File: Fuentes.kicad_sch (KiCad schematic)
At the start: 10 parts

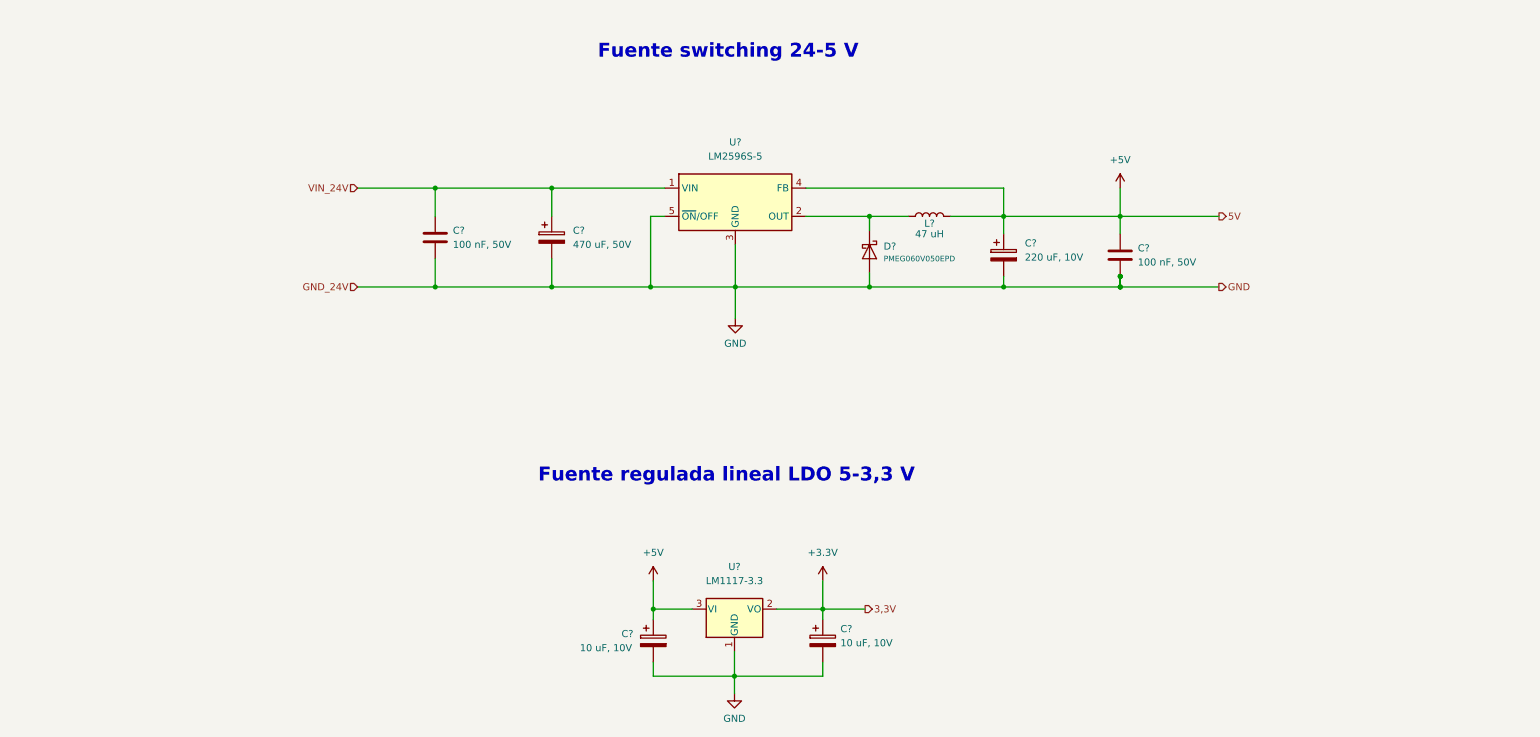
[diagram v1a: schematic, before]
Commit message: Actualización de SCH según placa industrial, y búsqueda de footprints.
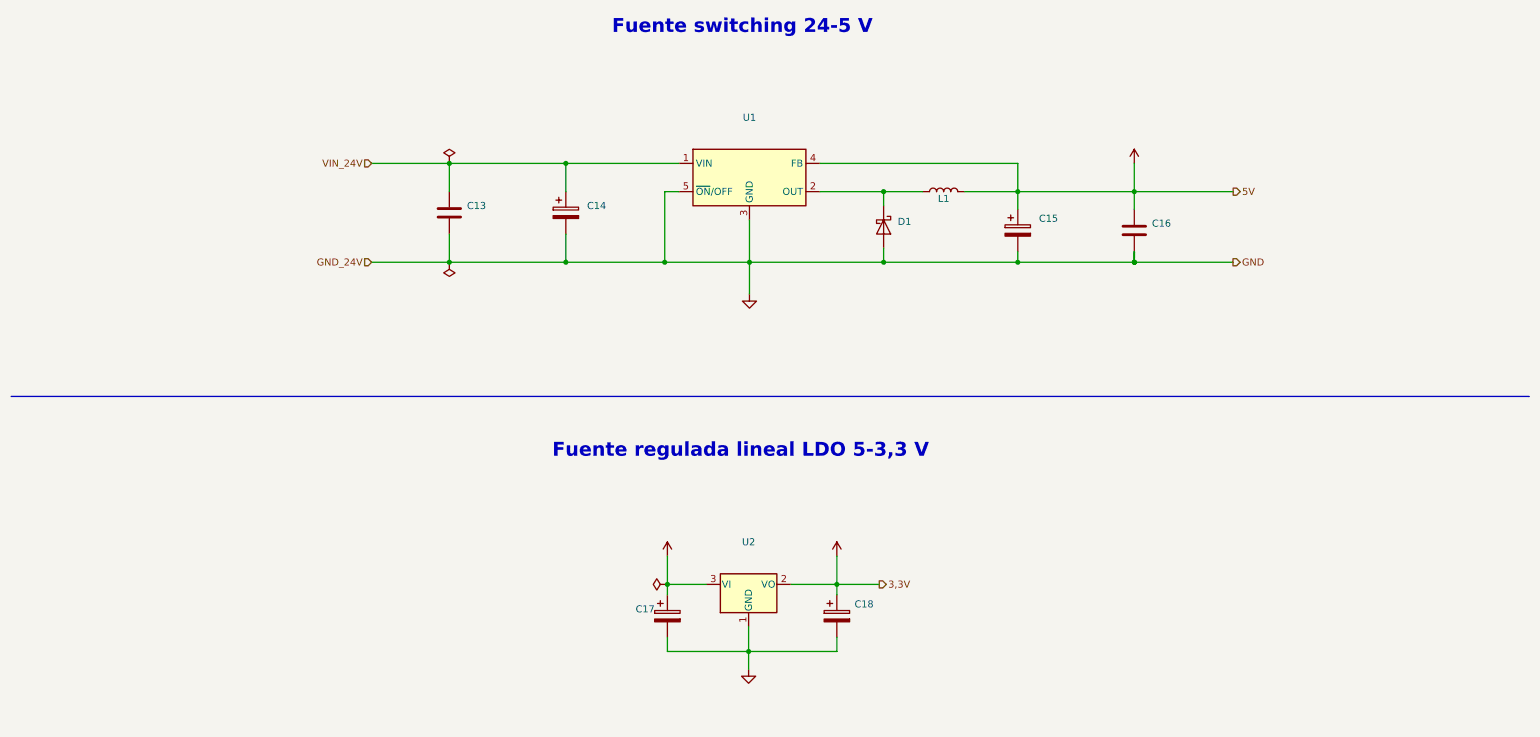
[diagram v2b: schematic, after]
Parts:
- removed C? (x2): 10 uF, 10V, symbol Device:C_Polarized
- removed C? (x2): 100 nF, 50V, symbol Device:C
- removed C?: 220 uF, 10V, symbol Device:C_Polarized
- removed C?: 470 uF, 50V, symbol Device:C_Polarized
- removed D?: PMEG060V050EPD, Package_TO_SOT_SMD:Nexperia_CFP15_SOT-1289, symbol Diode:PMEG060V050EPD
- removed L?: 47 uH, Inductor_SMD:L_0805_2012Metric, symbol Device:L
- removed U?: LM1117-3.3, symbol Regulator_Linear:LM1117-3.3
- removed U?: LM2596S-5, Package_TO_SOT_SMD:TO-263-5_TabPin3, symbol Regulator_Switching:LM2596S-5
- added C13, C16: (no value), Capacitor_SMD:C_0805_2012Metric, symbol Device:C
- added C14, C15: (no value), symbol Device:C_Polarized
- added C17, C18: (no value), Capacitor_SMD:C_0805_2012Metric, symbol Device:C_Polarized
- added D1: (no value), symbol Diode:PMEG060V050EPD
- added L1: (no value), symbol Device:L
- added U1: (no value), symbol Regulator_Switching:LM2596S-5
- added U2: (no value), symbol Regulator_Linear:LM1117-3.3
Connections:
- net +3.3V: now also C18.1, U2.2 (VO)
- net +5V: now also C15.1, C16.1, C17.1, L1.2, U1.4 (FB), U2.3 (VI)
- net GND: now also C13.2, C14.2, C15.2, C16.2, C17.2, C18.2, D1.1 (A), D1.2 (A), U1.3 (GND), U1.5 (~{ON}/OFF), U2.1 (GND)
- net VIN_24V: now also C13.1, C14.1, U1.1 (VIN)
- new net: D1.3 (K), L1.1, U1.2 (OUT)

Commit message: Fin de SCH, config de inicio para PCB
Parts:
- C13, C16: value (none) -> 100 nF, 50V
- C14: value (none) -> 470 uF, 50V; footprint (none) -> UUG1H471MNQ6MS:CAPAE1710X1750N
- C15: value (none) -> 220 uF, 10V; footprint (none) -> TPSE227K010R0100:TPSE227K016R0100V
- C17, C18: value (none) -> 10 uF, 10V
- D1: value (none) -> PMEG060V050EPD; footprint (none) -> Package_TO_SOT_SMD:Nexperia_CFP15_SOT-1289
- L1: value (none) -> 47 uH; footprint (none) -> 7447709470:WE-PD_1260_1245_1280_121054
- U1: value (none) -> LM2596S-5; footprint (none) -> Package_TO_SOT_SMD:TO-263-5_TabPin3
- U2: value (none) -> LM1117-3.3; footprint (none) -> LM1117MPX-33NOPB:SOT230P700X180-4N
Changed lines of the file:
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@@
       (effects (font (size 1.27 1.27)) (justify left))
     )
-    (property "Value" "" (id 1) (at 217.17 62.865 0)
+    (property "Value" "100 nF, 50V" (id 1) (at 217.17 62.865 0)
       (effects (font (size 1.27 1.27)) (justify left))
     )
@@
       (effects (font (size 1.27 1.27)) (justify left))
     )
-    (property "Value" "" (id 1) (at 115.57 59.69 0)
-      (effects (font (size 1.27 1.27)) (justify left))
-    )
-    (property "Footprint" "" (id 2) (at 112.7252 62.23 0)
+    (property "Value" "470 uF, 50V" (id 1) (at 115.57 59.69 0)
+      (effects (font (size 1.27 1.27)) (justify left))
+    )
+    (property "Footprint" "UUG1H471MNQ6MS:CAPAE1710X1750N" (id 2) (at 112.7252 62.23 0)
       (effects (font (size 1.27 1.27)) hide)
     )
@@
     (in_bom yes) (on_board yes) (fields_autoplaced)
     (property "Reference" "U2" (id 0) (at 144.6276 117.6274 0))
-    (property "Value" "" (id 1) (at 144.6276 120.1674 0))
-    (property "Footprint" "" (id 2) (at 144.6276 125.2474 0)
+    (property "Value" "LM1117-3.3" (id 1) (at 144.6276 120.1674 0))
+    (property "Footprint" "LM1117MPX-33NOPB:SOT230P700X180-4N" (id 2) (at 144.6276 125.2474 0)
       (effects (font (size 1.27 1.27)) hide)
     )
@@
       (effects (font (size 1.27 1.27)) hide)
     )
-    (property "Value" "" (id 1) (at 144.6276 144.9324 0))
+    (property "Value" "GND" (id 1) (at 144.6276 144.9324 0))
     (property "Footprint" "" (id 2) (at 144.6276 140.4874 0)
       (effects (font (size 1.27 1.27)) hide)
@@
       (effects (font (size 1.27 1.27)) hide)
     )
-    (property "Value" "" (id 1) (at 130.0226 115.0874 0))
+    (property "Value" "+5V" (id 1) (at 130.0226 115.0874 0))
     (property "Footprint" "" (id 2) (at 130.0226 120.1674 0)
       (effects (font (size 1.27 1.27)) hide)
@@
       (effects (font (size 1.27 1.27)) hide)
     )
-    (property "Value" "" (id 1) (at 90.805 44.45 0))
+    (property "Value" "PWR_FLAG" (id 1) (at 90.805 44.45 0))
     (property "Footprint" "" (id 2) (at 90.805 49.53 0)
       (effects (font (size 1.27 1.27)) hide)
@@
       (effects (font (size 1.27 1.27)) hide)
     )
-    (property "Value" "" (id 1) (at 122.555 125.095 90))
+    (property "Value" "PWR_FLAG" (id 1) (at 122.555 125.095 90))
     (property "Footprint" "" (id 2) (at 130.0226 125.2474 0)
       (effects (font (size 1.27 1.27)) hide)
@@
       (effects (font (size 1.27 1.27)) hide)
     )
-    (property "Value" "" (id 1) (at 213.995 44.45 0))
+    (property "Value" "+5V" (id 1) (at 213.995 44.45 0))
     (property "Footprint" "" (id 2) (at 213.995 49.53 0)
       (effects (font (size 1.27 1.27)) hide)
@@
     (in_bom yes) (on_board yes)
     (property "Reference" "L1" (id 0) (at 179.705 55.88 90))
-    (property "Value" "" (id 1) (at 179.705 57.785 90))
-    (property "Footprint" "" (id 2) (at 179.705 54.61 0)
+    (property "Value" "47 uH" (id 1) (at 179.705 57.785 90))
+    (property "Footprint" "7447709470:WE-PD_1260_1245_1280_121054" (id 2) (at 179.705 54.61 0)
       (effects (font (size 1.27 1.27)) hide)
     )
@@
       (effects (font (size 1.27 1.27)) (justify left))
     )
-    (property "Value" "" (id 1) (at 171.45 62.23 90)
+    (property "Value" "PMEG060V050EPD" (id 1) (at 171.45 62.23 90)
       (effects (font (size 1 1)) (justify left))
     )
-    (property "Footprint" "" (id 2) (at 164.465 60.96 0)
+    (property "Footprint" "Package_TO_SOT_SMD:Nexperia_CFP15_SOT-1289" (id 2) (at 164.465 60.96 0)
       (effects (font (size 1.27 1.27)) hide)
     )
@@
       (effects (font (size 1.27 1.27)) (justify left))
     )
-    (property "Value" "" (id 1) (at 93.98 59.69 0)
+    (property "Value" "100 nF, 50V" (id 1) (at 93.98 59.69 0)
       (effects (font (size 1.27 1.27)) (justify left))
     )
@@
       (effects (font (size 1.27 1.27)) (justify left))
     )
-    (property "Value" "" (id 1) (at 163.6776 131.3433 0)
+    (property "Value" "10 uF, 10V" (id 1) (at 163.6776 131.3433 0)
       (effects (font (size 1.27 1.27)) (justify left))
     )
@@
       (effects (font (size 1.27 1.27)) (justify left))
     )
-    (property "Value" "" (id 1) (at 126.2126 132.2324 0)
+    (property "Value" "10 uF, 10V" (id 1) (at 126.2126 132.2324 0)
       (effects (font (size 1.27 1.27)) (justify right))
     )
@@
       (effects (font (size 1.27 1.27)) hide)
     )
-    (property "Value" "" (id 1) (at 144.78 77.47 0))
+    (property "Value" "GND" (id 1) (at 144.78 77.47 0))
     (property "Footprint" "" (id 2) (at 144.78 73.025 0)
       (effects (font (size 1.27 1.27)) hide)
@@
     (in_bom yes) (on_board yes) (fields_autoplaced)
     (property "Reference" "U1" (id 0) (at 144.78 41.275 0))
-    (property "Value" "" (id 1) (at 144.78 43.815 0))
-    (property "Footprint" "" (id 2) (at 146.05 58.42 0)
+    (property "Value" "LM2596S-5" (id 1) (at 144.78 43.815 0))
+    (property "Footprint" "Package_TO_SOT_SMD:TO-263-5_TabPin3" (id 2) (at 146.05 58.42 0)
       (effects (font (size 1.27 1.27) italic) (justify left) hide)
     )
@@
       (effects (font (size 1.27 1.27)) hide)
     )
-    (property "Value" "" (id 1) (at 160.5026 115.0874 0))
+    (property "Value" "+3.3V" (id 1) (at 160.5026 115.0874 0))
     (property "Footprint" "" (id 2) (at 160.5026 120.1674 0)
       (effects (font (size 1.27 1.27)) hide)
@@
       (effects (font (size 1.27 1.27)) (justify left))
     )
-    (property "Value" "" (id 1) (at 196.85 61.9759 0)
-      (effects (font (size 1.27 1.27)) (justify left))
-    )
-    (property "Footprint" "" (id 2) (at 194.0052 65.405 0)
+    (property "Value" "220 uF, 10V" (id 1) (at 196.85 61.9759 0)
+      (effects (font (size 1.27 1.27)) (justify left))
+    )
+    (property "Footprint" "TPSE227K010R0100:TPSE227K016R0100V" (id 2) (at 194.0052 65.405 0)
       (effects (font (size 1.27 1.27)) hide)
     )
@@
       (effects (font (size 1.27 1.27)) hide)
     )
-    (property "Value" "" (id 1) (at 92.71 68.5799 0)
+    (property "Value" "PWR_FLAG" (id 1) (at 92.71 68.5799 0)
       (effects (font (size 1.27 1.27)) (justify right))
     )

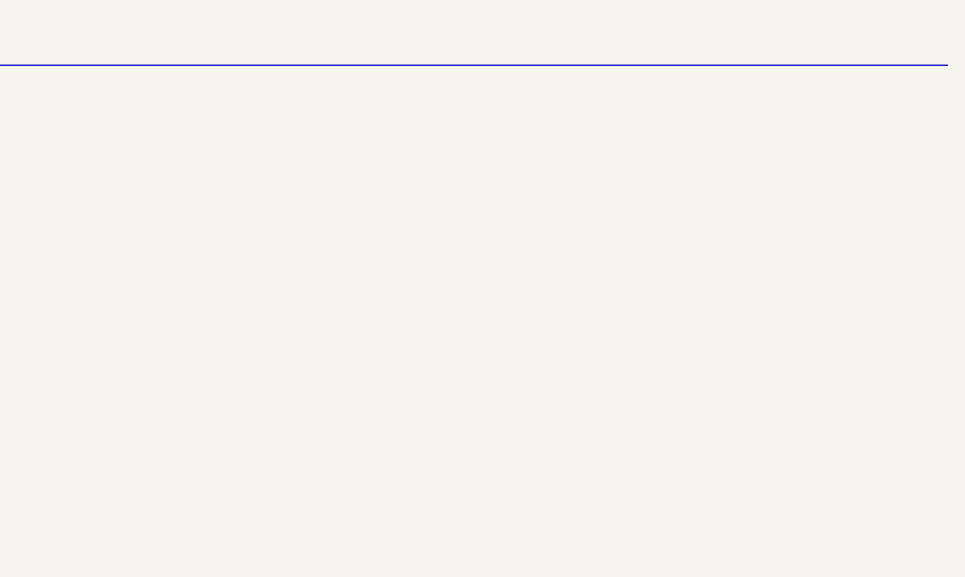
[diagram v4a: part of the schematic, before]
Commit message: Se finalizó con el PCB del prototipo.
Dado que se buscó a toda costa que el PCB fuera de 1 capa, en varios puntos del circuito se tuvieron que agregar pin headers individuales para conectar a 3V3 y GND, junto con tiras de pin headers. Cada una de estas se conectara luego entre si mediante cables.

Tambien se generaron los archivos Gerber y BOM.
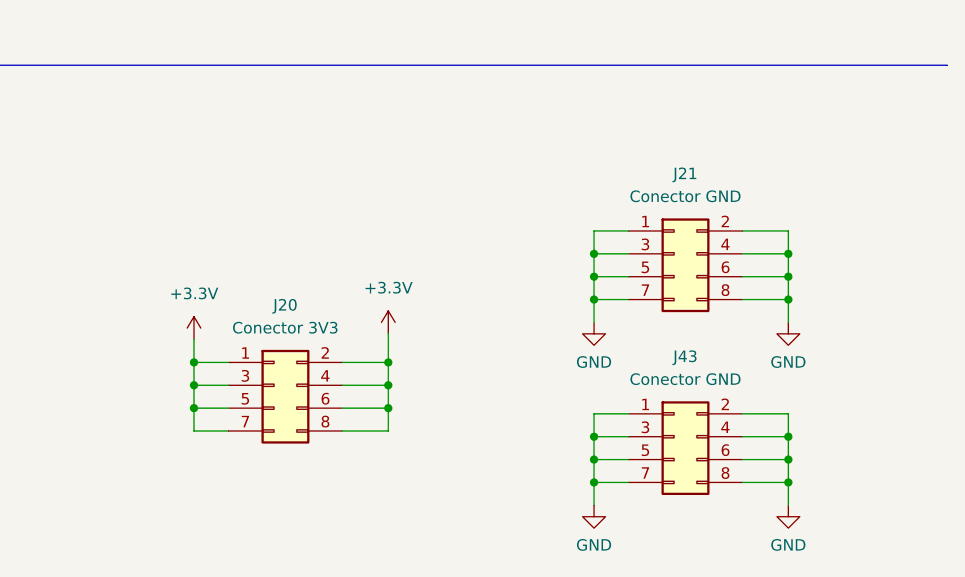
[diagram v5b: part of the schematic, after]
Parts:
- added J20: Conector 3V3, symbol Connector_Generic:Conn_02x04_Odd_Even
- added J21, J43: Conector GND, Connector_PinHeader_2.54mm:PinHeader_2x04_P2.54mm_Vertical, symbol Connector_Generic:Conn_02x04_Odd_Even
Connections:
- net +3.3V: now also J20.1 (Pin_1), J20.2 (Pin_2), J20.3 (Pin_3), J20.4 (Pin_4), J20.5 (Pin_5), J20.6 (Pin_6), J20.7 (Pin_7), J20.8 (Pin_8)
- net GND: now also J21.1 (Pin_1), J21.2 (Pin_2), J21.3 (Pin_3), J21.4 (Pin_4), J21.5 (Pin_5), J21.6 (Pin_6), J21.7 (Pin_7), J21.8 (Pin_8), J43.1 (Pin_1), J43.2 (Pin_2), J43.3 (Pin_3), J43.4 (Pin_4), J43.5 (Pin_5), J43.6 (Pin_6), J43.7 (Pin_7), J43.8 (Pin_8)

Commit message: Se modificaron los footprints del capacitor de 470 uF y del LM1117.
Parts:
- C14: footprint UUG1H471MNQ6MS:CAPAE1710X1750N -> VE-471M1HTR-1316:CAPAE1300X1650N
- J20: footprint (none) -> Connector_PinHeader_2.54mm:PinHeader_2x04_P2.54mm_Vertical
- U2: footprint LM1117MPX-33NOPB:SOT230P700X180-4N -> LM1117SX-3V3-NOPB:KTT0003B
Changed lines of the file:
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@@
       (effects (font (size 1.27 1.27)) (justify left))
     )
-    (property "Footprint" "UUG1H471MNQ6MS:CAPAE1710X1750N" (id 2) (at 112.7252 62.23 0)
+    (property "Footprint" "VE-471M1HTR-1316:CAPAE1300X1650N" (id 2) (at 112.7252 62.23 0)
       (effects (font (size 1.27 1.27)) hide)
     )
@@
     (property "Reference" "U2" (id 0) (at 144.6276 117.6274 0))
     (property "Value" "LM1117-3.3" (id 1) (at 144.6276 120.1674 0))
-    (property "Footprint" "LM1117MPX-33NOPB:SOT230P700X180-4N" (id 2) (at 144.6276 125.2474 0)
+    (property "Footprint" "LM1117SX-3V3-NOPB:KTT0003B" (id 2) (at 144.6276 125.2474 0)
       (effects (font (size 1.27 1.27)) hide)
     )
@@
     (property "Reference" "J20" (id 0) (at 211.455 118.11 0))
     (property "Value" "Conector 3V3" (id 1) (at 211.455 120.65 0))
-    (property "Footprint" "" (id 2) (at 210.185 127 0)
+    (property "Footprint" "Connector_PinHeader_2.54mm:PinHeader_2x04_P2.54mm_Vertical" (id 2) (at 210.185 127 0)
       (effects (font (size 1.27 1.27)) hide)
     )
